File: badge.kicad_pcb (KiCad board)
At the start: 2 copper layers, 85 x 55 mm, 49 parts, among them Q1 BC547, SW2 SW_Push, SW3 SW_Push, SW4 SW_Push, U1 XIAO-ESP32-C3-DIP, U2 MC34063AP, U3 TL072

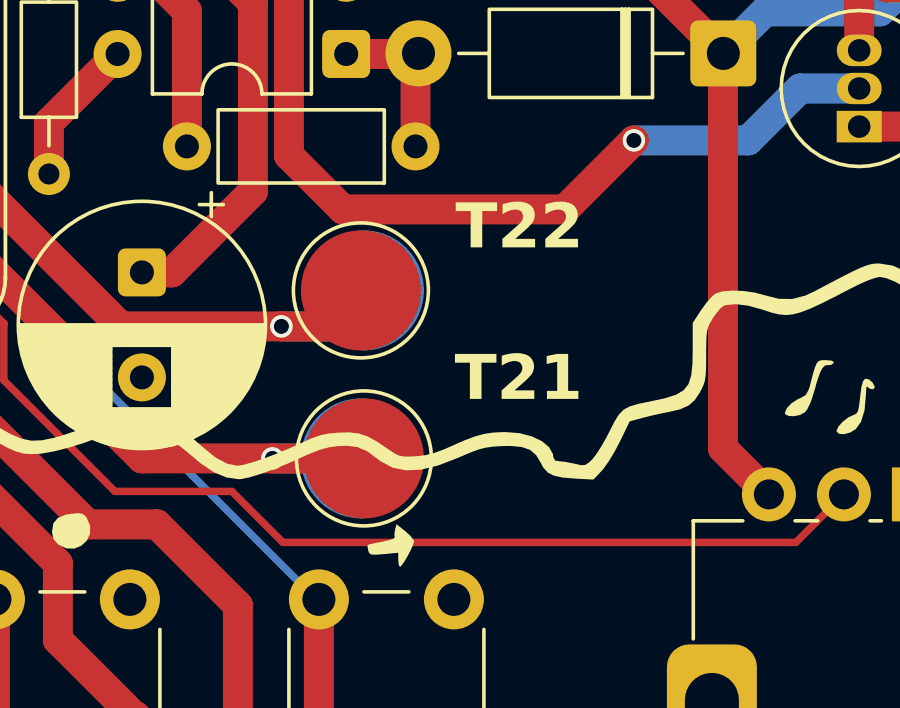
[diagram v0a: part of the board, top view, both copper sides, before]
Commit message: add qr
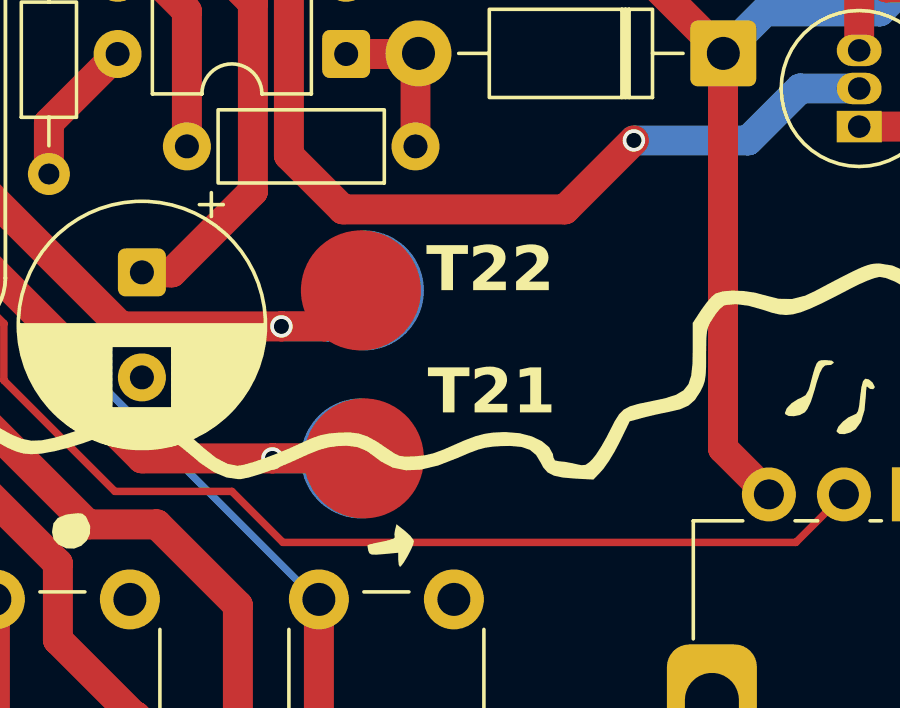
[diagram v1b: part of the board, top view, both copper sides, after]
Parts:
- added G***: LOGO, LOGO, B.Cu at (92.3, 119.2)
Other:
- board text added: "@Chris B"
